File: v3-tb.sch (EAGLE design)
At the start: 31 parts, among them U1 LMH6644MT, U2 LMH6642MF, U3 MAX5101, U4 PCAP04, U5 PMW3901, U6 VL53L1X, U7 BNO08X

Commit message: BNO08X stuff
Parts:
- added C18, C19: 22p, rcl:C-EUC0603
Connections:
- net GND: now also C18.2, C19.2, U7.CLKSEL0
- net N$11: now also C18.1
- net N$5: now also C19.1
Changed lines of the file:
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@@
 <part name="R7" library="rcl" library_urn="urn:adsk.eagle:library:334" deviceset="R-US_" device="R0603" package3d_urn="urn:adsk.eagle:package:23555/3" value="10k"/>
 <part name="+3V14" library="supply1" library_urn="urn:adsk.eagle:library:371" deviceset="+3V3" device=""/>
+<part name="GND26" library="supply1" library_urn="urn:adsk.eagle:library:371" deviceset="GND" device=""/>
+<part name="C18" library="rcl" library_urn="urn:adsk.eagle:library:334" deviceset="C-EU" device="C0603" package3d_urn="urn:adsk.eagle:package:23616/2" value="22p"/>
+<part name="C19" library="rcl" library_urn="urn:adsk.eagle:library:334" deviceset="C-EU" device="C0603" package3d_urn="urn:adsk.eagle:package:23616/2" value="22p"/>
+<part name="GND27" library="supply1" library_urn="urn:adsk.eagle:library:371" deviceset="GND" device=""/>
+<part name="GND28" library="supply1" library_urn="urn:adsk.eagle:library:371" deviceset="GND" device=""/>
 </parts>
 <sheets>
@@
 <attribute name="VALUE" x="358.14" y="129.54" size="1.778" layer="96" rot="R90"/>
 </instance>
+<instance part="GND26" gate="1" x="266.7" y="109.22" smashed="yes">
+<attribute name="VALUE" x="264.16" y="106.68" size="1.778" layer="96"/>
+</instance>
+<instance part="C18" gate="G$1" x="370.84" y="127" smashed="yes">
+<attribute name="NAME" x="372.364" y="127.381" size="1.778" layer="95"/>
+<attribute name="VALUE" x="372.364" y="122.301" size="1.778" layer="96"/>
+</instance>
+<instance part="C19" gate="G$1" x="386.08" y="127" smashed="yes">
+<attribute name="NAME" x="387.604" y="127.381" size="1.778" layer="95"/>
+<attribute name="VALUE" x="387.604" y="122.301" size="1.778" layer="96"/>
+</instance>
+<instance part="GND27" gate="1" x="370.84" y="116.84" smashed="yes">
+<attribute name="VALUE" x="368.3" y="114.3" size="1.778" layer="96"/>
+</instance>
+<instance part="GND28" gate="1" x="386.08" y="116.84" smashed="yes">
+<attribute name="VALUE" x="383.54" y="114.3" size="1.778" layer="96"/>
+</instance>
 </instances>
 <busses>
@@
 <pinref part="GND25" gate="1" pin="GND"/>
 <wire x1="347.98" y1="147.32" x2="350.52" y2="147.32" width="0.1524" layer="91"/>
+</segment>
+<segment>
+<pinref part="GND26" gate="1" pin="GND"/>
+<wire x1="266.7" y1="111.76" x2="266.7" y2="119.38" width="0.1524" layer="91"/>
+<pinref part="U7" gate="G$1" pin="CLKSEL0"/>
+<wire x1="266.7" y1="119.38" x2="269.24" y2="119.38" width="0.1524" layer="91"/>
+</segment>
+<segment>
+<pinref part="C18" gate="G$1" pin="2"/>
+<pinref part="GND27" gate="1" pin="GND"/>
+<wire x1="370.84" y1="119.38" x2="370.84" y2="121.92" width="0.1524" layer="91"/>
+</segment>
+<segment>
+<pinref part="C19" gate="G$1" pin="2"/>
+<pinref part="GND28" gate="1" pin="GND"/>
+<wire x1="386.08" y1="119.38" x2="386.08" y2="121.92" width="0.1524" layer="91"/>
 </segment>
 </net>
@@
 <segment>
 <pinref part="U7" gate="G$1" pin="XIN32"/>
-<wire x1="325.12" y1="142.24" x2="370.84" y2="142.24" width="0.1524" layer="91"/>
+<wire x1="325.12" y1="142.24" x2="386.08" y2="142.24" width="0.1524" layer="91"/>
+<pinref part="C19" gate="G$1" pin="1"/>
+<wire x1="386.08" y1="142.24" x2="386.08" y2="129.54" width="0.1524" layer="91"/>
 </segment>
 </net>
@@
 <pinref part="U7" gate="G$1" pin="CLKSEL1/XOUT32"/>
 <wire x1="325.12" y1="139.7" x2="370.84" y2="139.7" width="0.1524" layer="91"/>
-</segment>
-</net>
+<pinref part="C18" gate="G$1" pin="1"/>
+<wire x1="370.84" y1="139.7" x2="370.84" y2="129.54" width="0.1524" layer="91"/>
+</segment>
+</net>

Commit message: Adding headers
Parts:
- added J1: MPU_SPI, pinhead:PINHD-1X3
- added J10: HRDAC, pinhead:PINHD-1X2
- added J11: AMPS, pinhead:PINHD-1X5
- added J12: CDC_PC, pinhead:PINHD-1X6
- added J2: MCU_SPI, pinhead:PINHD-1X3
- added J3: MPU_I2C, pinhead:PINHD-1X2
- added J4: (no value), pinhead:PINHD-1X7
- added J5: (no value), pinhead:PINHD-1X5
- added J6: (no value), pinhead:PINHD-1X1
- added J7: POWER, pinhead:PINHD-1X3
- added J8: RGB_D, pinhead:PINHD-1X8
- added J9: RGB_A, pinhead:PINHD-1X2
- added Y1: 32.768k, crystal:FC-12M
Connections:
- net +1V8: now also J7.2
- net +3V3: now also J7.1
- net GND: now also J7.3
- net MISO: now also J1.1, J2.1
- net MOSI: now also J1.2, J2.2
- net N$11: now also Y1.1
- net N$5: now also Y1.2
- net SCK: now also J1.3, J2.3
- net SCL: now also J3.1
- net SDA: now also J3.2

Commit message: Finish headers
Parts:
- added J13: GROUND, pinhead:PINHD-1X3
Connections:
- new net RGB_D4: J8.5
- net AMP_B: now also J11.5
- net AMP_G: now also J11.4
- net AMP_R: now also J11.3
- net AMP_X: now also J11.1
- net AMP_Y: now also J11.2
- net CDC_PC0: now also J12.1
- net CDC_PC1: now also J12.2
- net CDC_PC2: now also J12.3
- net CDC_PC3: now also J12.4
- net CDC_PC4: now also J12.5
- net CDC_PC5: now also J12.6
- net GND: now also J13.1, J13.2, J13.3
- net HRDAC_X: now also J10.1
- net HRDAC_Y: now also J10.2
- net MCU_CDC_!CS: now also J5.1
- net MCU_CDC_PG2: now also J5.2
- net MCU_CDC_PG3: now also J5.3
- net MCU_CDC_PG4: now also J5.4
- net MCU_CDC_PG5: now also J5.5
- net MPU_IMU_!BOOT: now also J4.7
- net MPU_IMU_!CS: now also J4.4
- net MPU_IMU_!INT: now also J4.6
- net MPU_IMU_!RST: now also J4.5
- net MPU_OMT_!CS: now also J4.1
- net MPU_OMT_!INT: now also J4.3
- net MPU_OMT_!RST: now also J4.2
- net MPU_TOF_!INT: now also J6.1
- net RGB_A0: now also J9.1
- net RGB_A1: now also J9.2
- net RGB_D0: now also J8.1
- net RGB_D1: now also J8.2
- net RGB_D2: now also J8.3
- net RGB_D3: now also J8.4
- net RGB_D5: now also J8.6
- net RGB_D6: now also J8.7
- net RGB_D7: now also J8.8
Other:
- moved on the sheet: J11, J12, J4, J5, J6

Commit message: Finish headers
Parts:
- J4: value (none) -> MPU_SPI
- J5: value (none) -> MCU_SPI
- J6: device pinhead:PINHD-1X1 -> pinhead:PINHD-1X2
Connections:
- removed net MPU_TOF_!INT: J6.1, U6.GPIO1
- new net MPU_TOF_GPIO: J6.2, U6.GPIO1
- net RGB_!WR: now also J6.1
- net RGB_D3: no longer U3.D4
- net RGB_D4: now also U3.D4
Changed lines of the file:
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@@
 <part name="J2" library="pinhead" library_urn="urn:adsk.eagle:library:325" deviceset="PINHD-1X3" device="" package3d_urn="urn:adsk.eagle:package:22458/2" value="MCU_SPI"/>
 <part name="J3" library="pinhead" library_urn="urn:adsk.eagle:library:325" deviceset="PINHD-1X2" device="" package3d_urn="urn:adsk.eagle:package:22435/2" value="MPU_I2C"/>
-<part name="J4" library="pinhead" library_urn="urn:adsk.eagle:library:325" deviceset="PINHD-1X7" device="" package3d_urn="urn:adsk.eagle:package:22477/2"/>
-<part name="J5" library="pinhead" library_urn="urn:adsk.eagle:library:325" deviceset="PINHD-1X5" device="" package3d_urn="urn:adsk.eagle:package:22469/2"/>
-<part name="J6" library="pinhead" library_urn="urn:adsk.eagle:library:325" deviceset="PINHD-1X1" device="" package3d_urn="urn:adsk.eagle:package:22485/2"/>
+<part name="J4" library="pinhead" library_urn="urn:adsk.eagle:library:325" deviceset="PINHD-1X7" device="" package3d_urn="urn:adsk.eagle:package:22477/2" value="MPU_SPI"/>
+<part name="J5" library="pinhead" library_urn="urn:adsk.eagle:library:325" deviceset="PINHD-1X5" device="" package3d_urn="urn:adsk.eagle:package:22469/2" value="MCU_SPI"/>
 <part name="J7" library="pinhead" library_urn="urn:adsk.eagle:library:325" deviceset="PINHD-1X3" device="" package3d_urn="urn:adsk.eagle:package:22458/2" value="POWER"/>
 <part name="J8" library="pinhead" library_urn="urn:adsk.eagle:library:325" deviceset="PINHD-1X8" device="" package3d_urn="urn:adsk.eagle:package:22409/2" value="RGB_D"/>
@@
 <part name="J13" library="pinhead" library_urn="urn:adsk.eagle:library:325" deviceset="PINHD-1X3" device="" package3d_urn="urn:adsk.eagle:package:22458/2" value="GROUND"/>
 <part name="GND30" library="supply1" library_urn="urn:adsk.eagle:library:371" deviceset="GND" device=""/>
+<part name="J6" library="pinhead" library_urn="urn:adsk.eagle:library:325" deviceset="PINHD-1X2" device="" package3d_urn="urn:adsk.eagle:package:22435/2"/>
 </parts>
 <sheets>
@@
 <attribute name="VALUE" x="499.11" y="147.32" size="1.778" layer="96"/>
 </instance>
-<instance part="J6" gate="G$1" x="505.46" y="139.7" smashed="yes">
-<attribute name="NAME" x="499.11" y="142.875" size="1.778" layer="95"/>
-<attribute name="VALUE" x="499.11" y="134.62" size="1.778" layer="96"/>
-</instance>
 <instance part="J7" gate="A" x="459.74" y="223.52" smashed="yes">
 <attribute name="NAME" x="453.39" y="229.235" size="1.778" layer="95"/>
@@
 <instance part="GND30" gate="1" x="474.98" y="215.9" smashed="yes">
 <attribute name="VALUE" x="472.44" y="213.36" size="1.778" layer="96"/>
+</instance>
+<instance part="J6" gate="G$1" x="505.46" y="137.16" smashed="yes">
+<attribute name="NAME" x="499.11" y="142.875" size="1.778" layer="95"/>
+<attribute name="VALUE" x="499.11" y="132.08" size="1.778" layer="96"/>
 </instance>
 </instances>
@@
 <pinref part="U3" gate="G$1" pin="D3"/>
 <wire x1="38.1" y1="66.04" x2="35.56" y2="66.04" width="0.1524" layer="91"/>
-</segment>
-<segment>
-<pinref part="U3" gate="G$1" pin="D4"/>
-<wire x1="38.1" y1="63.5" x2="35.56" y2="63.5" width="0.1524" layer="91"/>
 </segment>
 <segment>
@@
 <wire x1="68.58" y1="55.88" x2="78.74" y2="55.88" width="0.1524" layer="91"/>
 <label x="68.58" y="55.88" size="1.778" layer="95"/>
+</segment>
+<segment>
+<pinref part="J6" gate="G$1" pin="1"/>
+<wire x1="502.92" y1="139.7" x2="490.22" y2="139.7" width="0.1524" layer="91"/>
+<label x="485.14" y="139.7" size="1.778" layer="95"/>
 </segment>
 </net>
@@
 </segment>
 </net>
-<net name="MPU_TOF_!INT" class="0">
-<segment>
-<pinref part="U6" gate="G$1" pin="GPIO1"/>
-<wire x1="180.34" y1="182.88" x2="165.1" y2="182.88" width="0.1524" layer="91"/>
-<label x="162.56" y="182.88" size="1.778" layer="95"/>
-</segment>
-<segment>
-<pinref part="J6" gate="G$1" pin="1"/>
-<wire x1="502.92" y1="139.7" x2="490.22" y2="139.7" width="0.1524" layer="91"/>
-<label x="480.06" y="139.7" size="1.778" layer="95"/>
-</segment>
-</net>
 <net name="MCU_CDC_PG2" class="0">
 <segment>
@@
 <wire x1="449.58" y1="88.9" x2="457.2" y2="88.9" width="0.1524" layer="91"/>
 </segment>
-</net>
+<segment>
+<pinref part="U3" gate="G$1" pin="D4"/>
+<wire x1="38.1" y1="63.5" x2="35.56" y2="63.5" width="0.1524" layer="91"/>
+</segment>
+</net>
+<net name="MPU_TOF_GPIO" class="0">
+<segment>
+<pinref part="U6" gate="G$1" pin="GPIO1"/>
+<wire x1="180.34" y1="182.88" x2="165.1" y2="182.88" width="0.1524" layer="91"/>
+<label x="160.02" y="182.88" size="1.778" layer="95"/>
+</segment>
+<segment>
+<wire x1="502.92" y1="137.16" x2="490.22" y2="137.16" width="0.1524" layer="91"/>
+<label x="477.52" y="137.16" size="1.778" layer="95"/>
+<pinref part="J6" gate="G$1" pin="2"/>
+</segment>
+</net>

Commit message: Update headers
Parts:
- J4: value MPU_SPI -> MPU_ETC
- J5: value MCU_SPI -> MCU_ETC
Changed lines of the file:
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@@
 <part name="J2" library="pinhead" library_urn="urn:adsk.eagle:library:325" deviceset="PINHD-1X3" device="" package3d_urn="urn:adsk.eagle:package:22458/2" value="MCU_SPI"/>
 <part name="J3" library="pinhead" library_urn="urn:adsk.eagle:library:325" deviceset="PINHD-1X2" device="" package3d_urn="urn:adsk.eagle:package:22435/2" value="MPU_I2C"/>
-<part name="J4" library="pinhead" library_urn="urn:adsk.eagle:library:325" deviceset="PINHD-1X7" device="" package3d_urn="urn:adsk.eagle:package:22477/2" value="MPU_SPI"/>
-<part name="J5" library="pinhead" library_urn="urn:adsk.eagle:library:325" deviceset="PINHD-1X5" device="" package3d_urn="urn:adsk.eagle:package:22469/2" value="MCU_SPI"/>
+<part name="J4" library="pinhead" library_urn="urn:adsk.eagle:library:325" deviceset="PINHD-1X7" device="" package3d_urn="urn:adsk.eagle:package:22477/2" value="MPU_ETC"/>
+<part name="J5" library="pinhead" library_urn="urn:adsk.eagle:library:325" deviceset="PINHD-1X5" device="" package3d_urn="urn:adsk.eagle:package:22469/2" value="MCU_ETC"/>
 <part name="J7" library="pinhead" library_urn="urn:adsk.eagle:library:325" deviceset="PINHD-1X3" device="" package3d_urn="urn:adsk.eagle:package:22458/2" value="POWER"/>
 <part name="J8" library="pinhead" library_urn="urn:adsk.eagle:library:325" deviceset="PINHD-1X8" device="" package3d_urn="urn:adsk.eagle:package:22409/2" value="RGB_D"/>

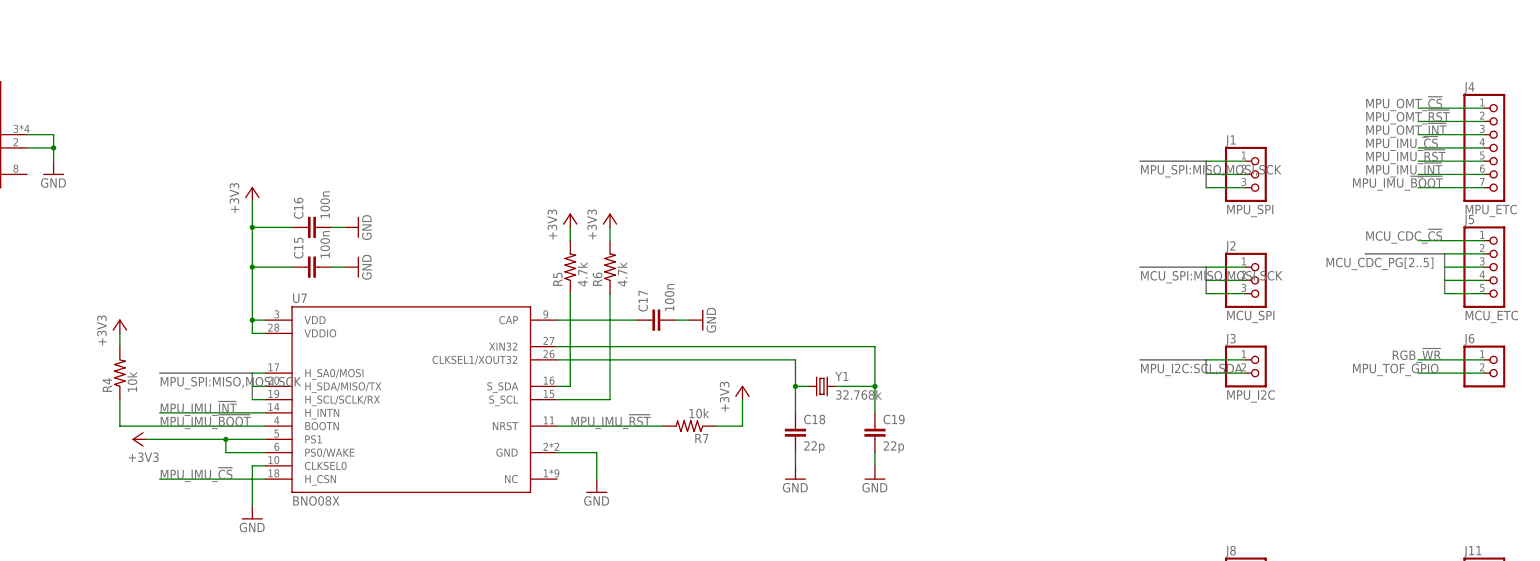
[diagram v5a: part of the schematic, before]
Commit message: Add WAKE pin on IMU
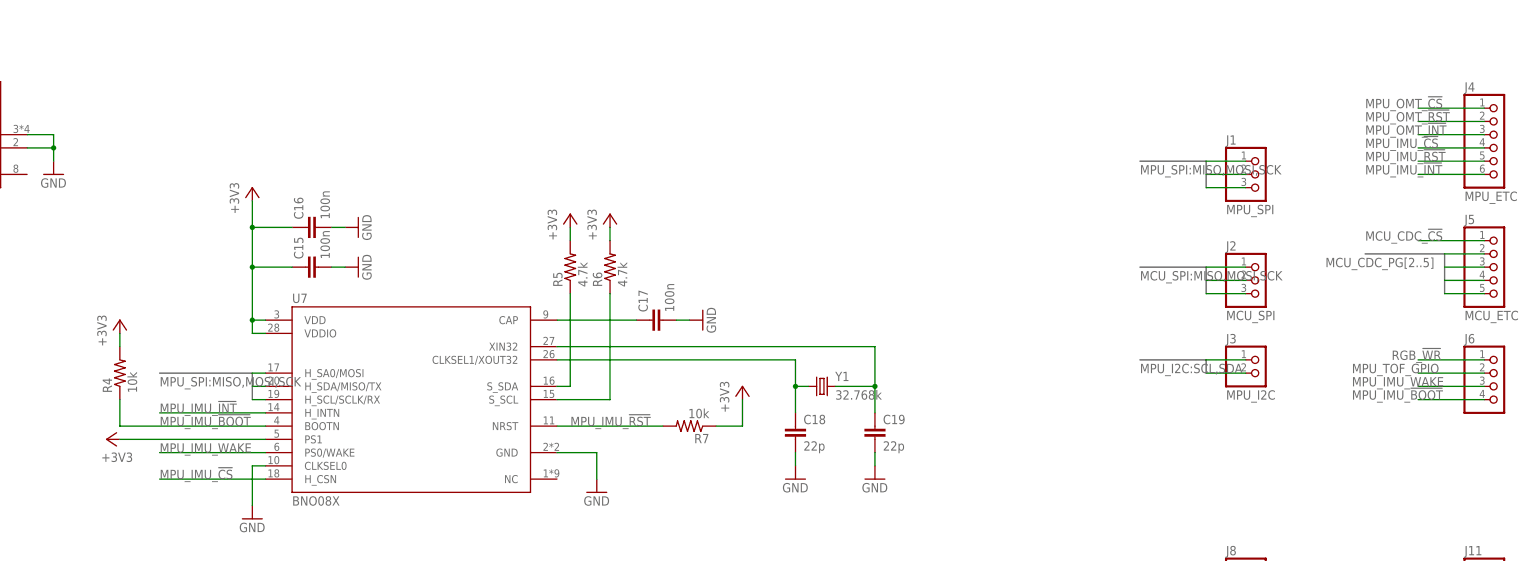
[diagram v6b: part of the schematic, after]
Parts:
- J4: device pinhead:PINHD-1X7 -> pinhead:PINHD-1X6
- J6: device pinhead:PINHD-1X2 -> pinhead:PINHD-1X4
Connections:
- new net MPU_IMU_WAKE: J6.3, U7.PS0/WAKE
- net +3V3: no longer U7.PS0/WAKE
- net MPU_IMU_!BOOT: now also J6.4; no longer J4.7
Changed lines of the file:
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@@
 <part name="J2" library="pinhead" library_urn="urn:adsk.eagle:library:325" deviceset="PINHD-1X3" device="" package3d_urn="urn:adsk.eagle:package:22458/2" value="MCU_SPI"/>
 <part name="J3" library="pinhead" library_urn="urn:adsk.eagle:library:325" deviceset="PINHD-1X2" device="" package3d_urn="urn:adsk.eagle:package:22435/2" value="MPU_I2C"/>
-<part name="J4" library="pinhead" library_urn="urn:adsk.eagle:library:325" deviceset="PINHD-1X7" device="" package3d_urn="urn:adsk.eagle:package:22477/2" value="MPU_ETC"/>
 <part name="J5" library="pinhead" library_urn="urn:adsk.eagle:library:325" deviceset="PINHD-1X5" device="" package3d_urn="urn:adsk.eagle:package:22469/2" value="MCU_ETC"/>
 <part name="J7" library="pinhead" library_urn="urn:adsk.eagle:library:325" deviceset="PINHD-1X3" device="" package3d_urn="urn:adsk.eagle:package:22458/2" value="POWER"/>
@@
 <part name="J13" library="pinhead" library_urn="urn:adsk.eagle:library:325" deviceset="PINHD-1X3" device="" package3d_urn="urn:adsk.eagle:package:22458/2" value="GROUND"/>
 <part name="GND30" library="supply1" library_urn="urn:adsk.eagle:library:371" deviceset="GND" device=""/>
-<part name="J6" library="pinhead" library_urn="urn:adsk.eagle:library:325" deviceset="PINHD-1X2" device="" package3d_urn="urn:adsk.eagle:package:22435/2"/>
+<part name="J4" library="pinhead" library_urn="urn:adsk.eagle:library:325" deviceset="PINHD-1X6" device="" package3d_urn="urn:adsk.eagle:package:22472/2" value="MPU_ETC"/>
+<part name="J6" library="pinhead" library_urn="urn:adsk.eagle:library:325" deviceset="PINHD-1X4" device="" package3d_urn="urn:adsk.eagle:package:22407/2"/>
 </parts>
 <sheets>
@@
 <attribute name="VALUE" x="289.56" y="162.56" size="1.778" layer="96" rot="R90"/>
 </instance>
-<instance part="+3V11" gate="G$1" x="243.84" y="124.46" smashed="yes" rot="R90">
-<attribute name="VALUE" x="248.92" y="121.92" size="1.778" layer="96" rot="R180"/>
+<instance part="+3V11" gate="G$1" x="238.76" y="124.46" smashed="yes" rot="R90">
+<attribute name="VALUE" x="243.84" y="121.92" size="1.778" layer="96" rot="R180"/>
 </instance>
 <instance part="R5" gate="G$1" x="327.66" y="157.48" smashed="yes" rot="R90">
@@
 <attribute name="VALUE" x="453.39" y="132.08" size="1.778" layer="96"/>
 </instance>
-<instance part="J4" gate="A" x="505.46" y="180.34" smashed="yes">
-<attribute name="NAME" x="499.11" y="191.135" size="1.778" layer="95"/>
-<attribute name="VALUE" x="499.11" y="167.64" size="1.778" layer="96"/>
-</instance>
 <instance part="J5" gate="A" x="505.46" y="157.48" smashed="yes">
 <attribute name="NAME" x="499.11" y="165.735" size="1.778" layer="95"/>
@@
 <attribute name="VALUE" x="472.44" y="213.36" size="1.778" layer="96"/>
 </instance>
-<instance part="J6" gate="G$1" x="505.46" y="137.16" smashed="yes">
+<instance part="J4" gate="A" x="505.46" y="180.34" smashed="yes">
+<attribute name="NAME" x="499.11" y="191.135" size="1.778" layer="95"/>
+<attribute name="VALUE" x="499.11" y="170.18" size="1.778" layer="96"/>
+</instance>
+<instance part="J6" gate="A" x="505.46" y="134.62" smashed="yes">
 <attribute name="NAME" x="499.11" y="142.875" size="1.778" layer="95"/>
-<attribute name="VALUE" x="499.11" y="132.08" size="1.778" layer="96"/>
+<attribute name="VALUE" x="499.11" y="127" size="1.778" layer="96"/>
 </instance>
 </instances>
@@
 </segment>
 <segment>
-<pinref part="J6" gate="G$1" pin="1"/>
 <wire x1="502.92" y1="139.7" x2="490.22" y2="139.7" width="0.1524" layer="91"/>
 <label x="485.14" y="139.7" size="1.778" layer="95"/>
+<pinref part="J6" gate="A" pin="1"/>
 </segment>
 </net>
@@
 </segment>
 <segment>
-<pinref part="U7" gate="G$1" pin="PS0/WAKE"/>
-<wire x1="269.24" y1="121.92" x2="261.62" y2="121.92" width="0.1524" layer="91"/>
-<wire x1="261.62" y1="121.92" x2="261.62" y2="124.46" width="0.1524" layer="91"/>
 <pinref part="+3V11" gate="G$1" pin="+3V3"/>
-<wire x1="261.62" y1="124.46" x2="246.38" y2="124.46" width="0.1524" layer="91"/>
+<wire x1="269.24" y1="124.46" x2="241.3" y2="124.46" width="0.1524" layer="91"/>
 <pinref part="U7" gate="G$1" pin="PS1"/>
-<wire x1="269.24" y1="124.46" x2="261.62" y2="124.46" width="0.1524" layer="91"/>
-<junction x="261.62" y="124.46"/>
 </segment>
 <segment>
@@
 </segment>
 <segment>
-<pinref part="J4" gate="A" pin="2"/>
 <wire x1="502.92" y1="185.42" x2="490.22" y2="185.42" width="0.1524" layer="91"/>
 <label x="480.06" y="185.42" size="1.778" layer="95"/>
+<pinref part="J4" gate="A" pin="2"/>
 </segment>
 </net>
@@
 </segment>
 <segment>
-<pinref part="J4" gate="A" pin="1"/>
 <wire x1="502.92" y1="187.96" x2="490.22" y2="187.96" width="0.1524" layer="91"/>
 <label x="480.06" y="187.96" size="1.778" layer="95"/>
+<pinref part="J4" gate="A" pin="1"/>
 </segment>
 </net>
@@
 </segment>
 <segment>
-<pinref part="J4" gate="A" pin="3"/>
 <wire x1="502.92" y1="182.88" x2="490.22" y2="182.88" width="0.1524" layer="91"/>
 <label x="480.06" y="182.88" size="1.778" layer="95"/>
+<pinref part="J4" gate="A" pin="3"/>
 </segment>
 </net>
@@
 </segment>
 <segment>
-<pinref part="J4" gate="A" pin="6"/>
 <wire x1="502.92" y1="175.26" x2="490.22" y2="175.26" width="0.1524" layer="91"/>
 <label x="480.06" y="175.26" size="1.778" layer="95"/>
+<pinref part="J4" gate="A" pin="6"/>
 </segment>
 </net>
@@
 </segment>
 <segment>
-<pinref part="J4" gate="A" pin="7"/>
-<wire x1="502.92" y1="172.72" x2="490.22" y2="172.72" width="0.1524" layer="91"/>
-<label x="477.52" y="172.72" size="1.778" layer="95"/>
+<wire x1="502.92" y1="132.08" x2="490.22" y2="132.08" width="0.1524" layer="91"/>
+<label x="477.52" y="132.08" size="1.778" layer="95"/>
+<pinref part="J6" gate="A" pin="4"/>
 </segment>
 </net>
@@
 </segment>
 <segment>
-<pinref part="J4" gate="A" pin="4"/>
 <wire x1="502.92" y1="180.34" x2="490.22" y2="180.34" width="0.1524" layer="91"/>
 <label x="480.06" y="180.34" size="1.778" layer="95"/>
+<pinref part="J4" gate="A" pin="4"/>
 </segment>
 </net>
@@
 </segment>
 <segment>
-<pinref part="J4" gate="A" pin="5"/>
 <wire x1="502.92" y1="177.8" x2="490.22" y2="177.8" width="0.1524" layer="91"/>
 <label x="480.06" y="177.8" size="1.778" layer="95"/>
+<pinref part="J4" gate="A" pin="5"/>
 </segment>
 </net>
@@
 <wire x1="502.92" y1="137.16" x2="490.22" y2="137.16" width="0.1524" layer="91"/>
 <label x="477.52" y="137.16" size="1.778" layer="95"/>
-<pinref part="J6" gate="G$1" pin="2"/>
-</segment>
-</net>
+<pinref part="J6" gate="A" pin="2"/>
+</segment>
+</net>
+<net name="MPU_IMU_WAKE" class="0">
+<segment>
+<pinref part="U7" gate="G$1" pin="PS0/WAKE"/>
+<wire x1="269.24" y1="121.92" x2="248.92" y2="121.92" width="0.1524" layer="91"/>
+<label x="248.92" y="121.92" size="1.778" layer="95"/>
+</segment>
+<segment>
+<wire x1="502.92" y1="134.62" x2="490.22" y2="134.62" width="0.1524" layer="91"/>
+<label x="477.52" y="134.62" size="1.778" layer="95"/>
+<pinref part="J6" gate="A" pin="3"/>
+</segment>
+</net>
